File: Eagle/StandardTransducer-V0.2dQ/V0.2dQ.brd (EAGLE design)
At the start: 59.2 x 58 mm, 72 parts, among them CON1 SPI, IC2 TL072D, IC3 LP298XS, IC4 LORA-RA_01_SOIC, J1 87758-0216, Q1 FDN360P, Q2 FDN360P, Q3 FDN360P, Q5 BSP75, U1 RN2483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

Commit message: New version of 0.2dQ
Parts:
- removed C6: 0.1uF, rcl:C0805
- removed L2: 10uH, rcl:L1812
- added Q4: FDN360P, transistor-power:SUPER-SOT3
- added R14: 1k, rcl:R0805
- added R19: 220k, rcl:R0805
- moved RK6 132.6 mm to (40.4, 42.9), turned to 90 degrees
- moved Q5 125.9 mm to (45.7, 43.2)
- moved SJ5 102.0 mm to (18.3, 33.7), turned to 180 degrees
- moved SJ4 102.0 mm to (39.9, 29.5), turned to 90 degrees
- moved Q3 73.1 mm to (7.24, 19.3), flipped to the bottom, turned to 270 degrees
- moved R18 67.3 mm to (10.4, 19.1), flipped to the bottom, turned to 270 degrees
- moved R16 63.6 mm to (8.51, 22.1), flipped to the bottom
- moved C10 10.4 mm to (48.8, 15.4), flipped to the bottom
- moved D2 8.92 mm to (50.5, 16.2)
- moved JP5 8.50 mm to (44.5, 21.3)
- moved F1 6.02 mm to (46.0, 15.5), turned to 270 degrees
- moved D4 5.67 mm to (46.0, 15.5)
- moved R4 1.57 mm to (13.6, 22.9), flipped to the bottom
- moved R5 1.20 mm to (13.2, 19.8), flipped to the bottom, turned to 90 degrees
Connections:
- removed net A3: U$4.39
- removed net DVCC: C6.1, L2.2, Q3.2, R10.1, R11.2, R12.2, R18.2, R8.1
- removed net N$1: F1.2, L1.1, L2.1
- new net AVCCOPA: IC2.8, Q4.3
- new net N$3: Q4.1, R14.1, R19.1
- new net VIN: C11.1, F1.2, IC3.1, J1.2, L1.1, R10.1, R11.2, R12.2, R8.1
- net ANGND: now also IC4.P$16, IC4.P$2, JP5.4
- net AVCC: now also Q4.2, R19.2; no longer IC2.8
- net D+3V3: now also Q3.2, R18.2, U$4.39
- net D10*: now also U$4.31; no longer U$4.30
- net D6*: now also U$4.28; no longer U$4.27
- net D7*: now also U$4.27; no longer U$4.1
- net D8*: now also U$4.29; no longer U$4.28
- net D9*: now also U$4.30; no longer U$4.29
- net GND: no longer C6.2, IC4.P$16, IC4.P$2, JP5.4
- net RA1/2483: now also U$4.1; no longer U$4.31
- net VCC: no longer C11.1, IC3.1, J1.2
- net VOPA: now also R14.2
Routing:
- net VIN: track 0.00 -> 145.8 mm, vias 0 -> 3
- net DVCC: track 143.3 -> 0.00 mm, vias 5 -> 0
- net VCC: track 136.2 -> 22.6 mm, vias 4 -> 1
- net AVCCOPA: track 0.00 -> 72.0 mm
- net TX: track 76.8 -> 34.6 mm, vias 6 -> 2
- net RX: track 69.3 -> 32.6 mm, vias 4 -> 1
- net SVANALOG: track 0.00 -> 22.1 mm, vias 0 -> 1
- net DVSENSORS: track 0.00 -> 20.7 mm, vias 0 -> 1
- net D7*: track 0.00 -> 20.3 mm
- net VSENSORS: track 66.4 -> 48.1 mm, vias 1 -> 0
- net ANGND: track 2.85 -> 18.4 mm, vias 0 -> 5
- net VOPA: track 0.00 -> 14.0 mm
- net N$1: track 13.2 -> 0.00 mm
- net RST: track 125.4 -> 138.4 mm
- net AVCC: track 45.6 -> 34.5 mm
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- added copper zone on layer 1, net ANGND
- added copper zone on layer 16, net ANGND
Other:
- board text added: "GND/AGND"
- board text added: "LORA/BLE"
- board text added: "RA1/2483"
- board text added: "RST"
- board text added: "StandTransducer V2.0"
- board text removed: "StandTransducer V1.0"

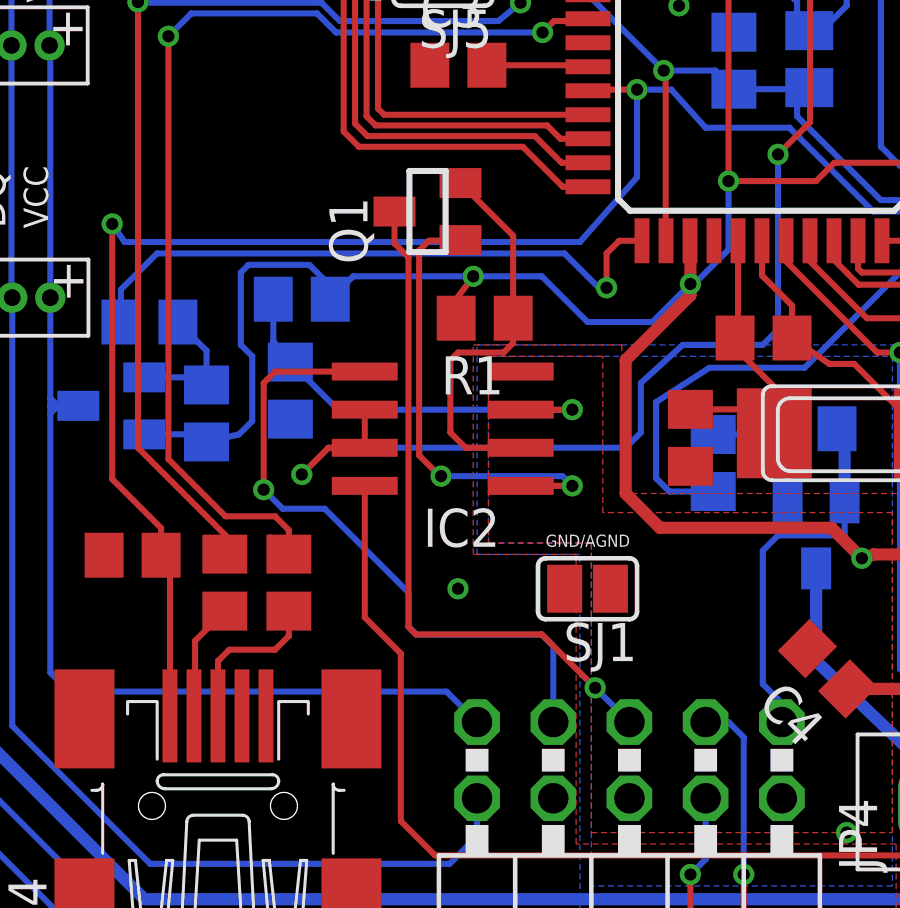
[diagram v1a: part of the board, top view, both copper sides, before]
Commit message: Change width to 16 mil for SVANALOG route.
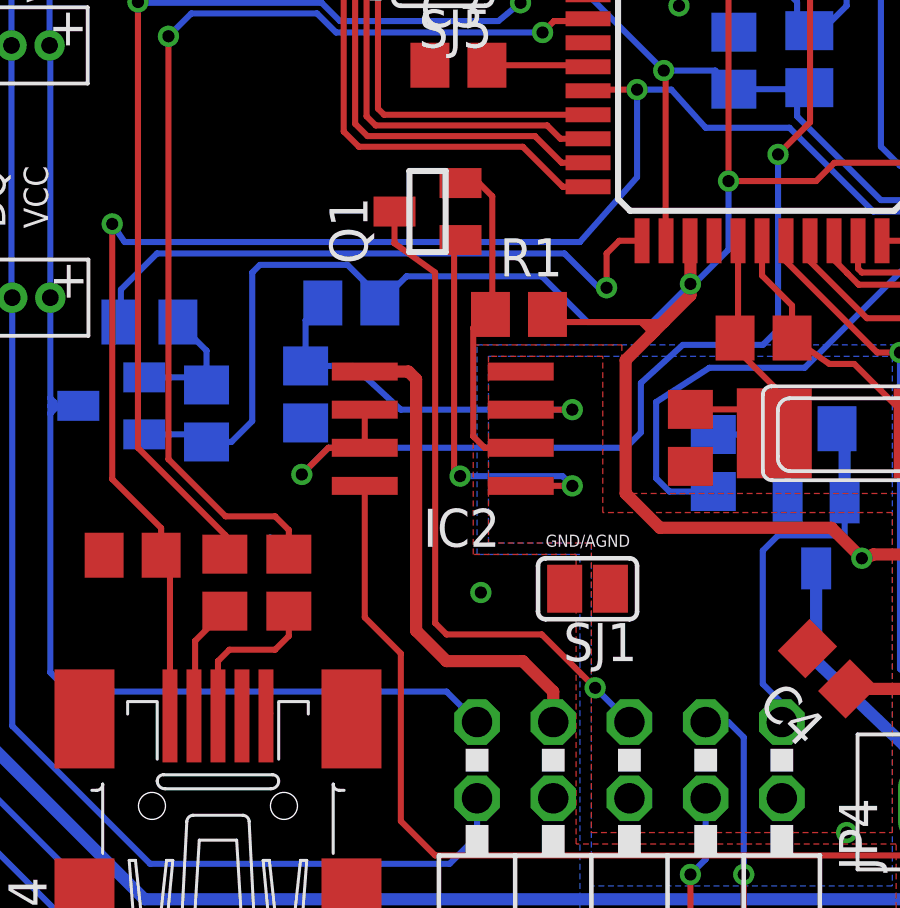
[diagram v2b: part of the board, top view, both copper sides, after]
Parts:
- moved R4 1.66 mm to (15.2, 22.7)
- moved R1 1.15 mm to (20.8, 22.4), turned to 0 degrees
- moved R5 0.52 mm to (13.7, 19.7)
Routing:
- net SVANALOG: track 22.1 -> 16.6 mm, vias 1 -> 0
- net D+3V3: track 189.5 -> 192.3 mm, vias 11 -> 10
- net N$5: track 13.4 -> 11.3 mm
- net N$2: track 15.6 -> 13.6 mm
- net N$4: track 14.1 -> 13.5 mm

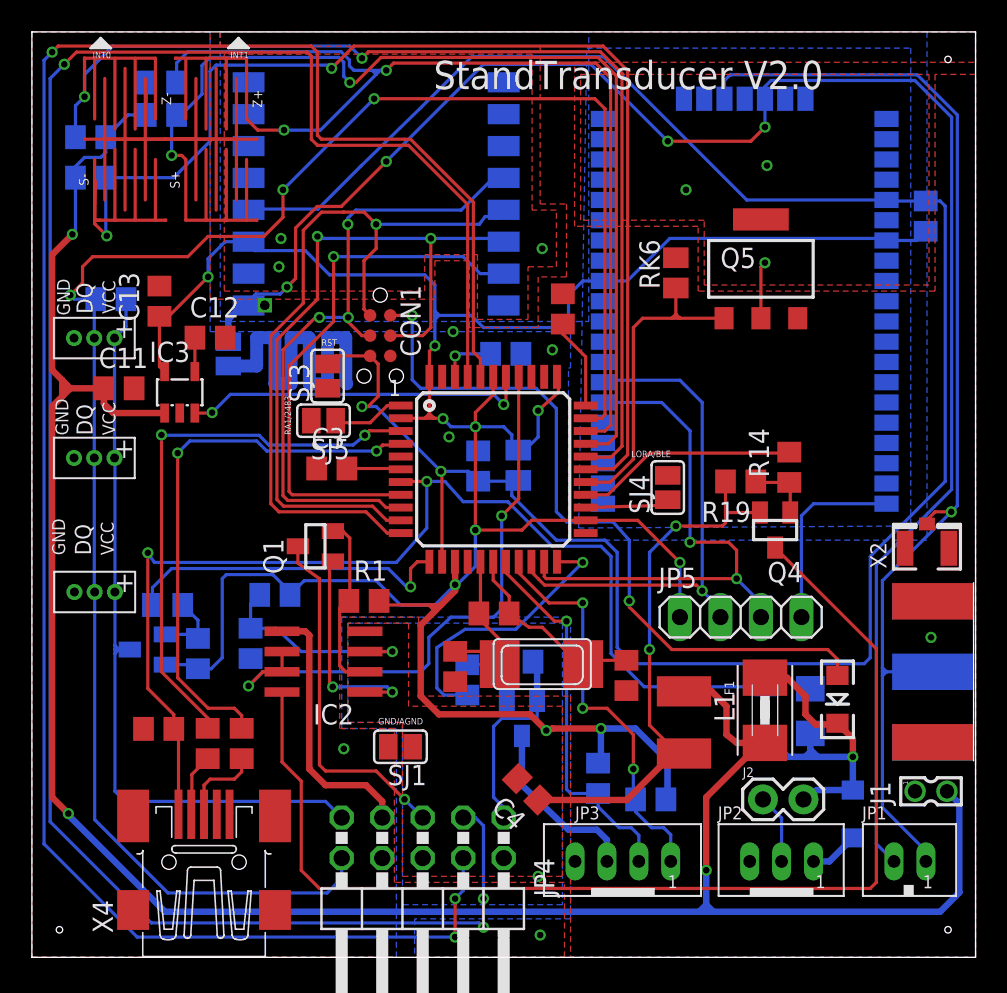
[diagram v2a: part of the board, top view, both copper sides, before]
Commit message: Changes width for VCCOPA and SVANALOG
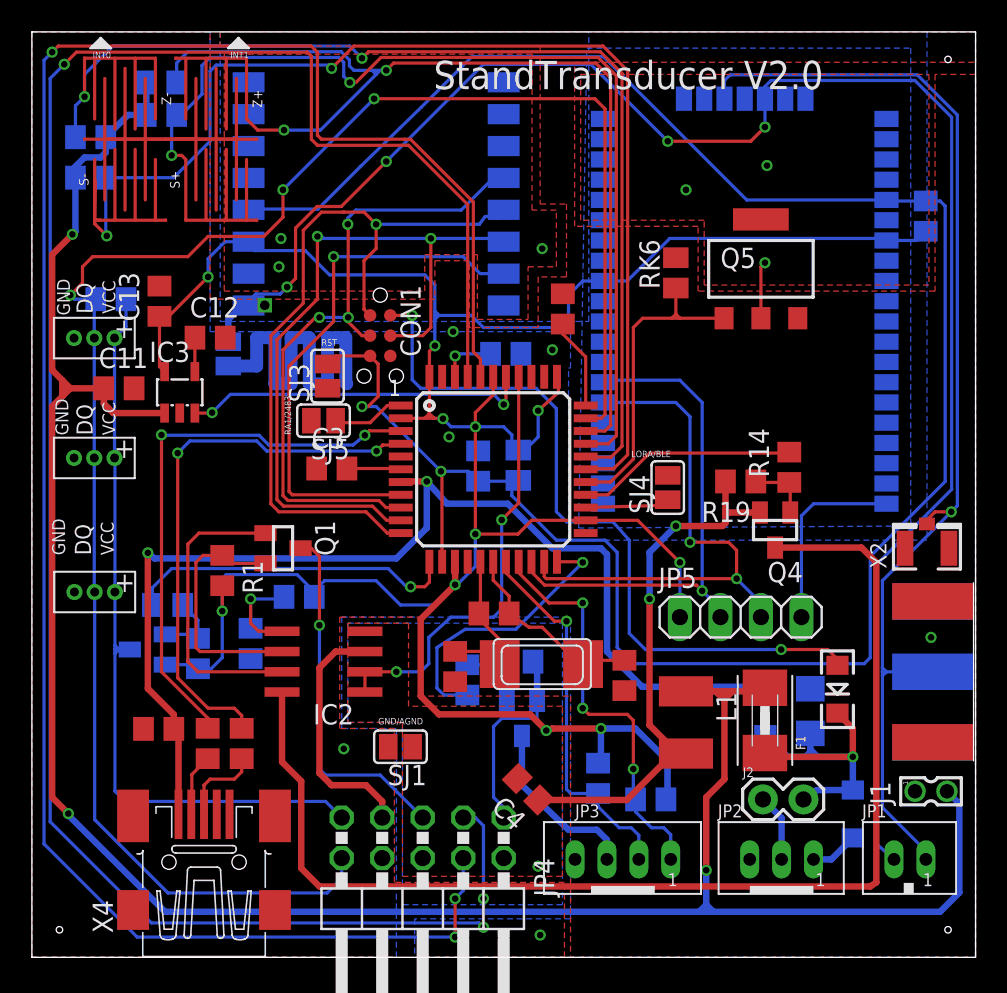
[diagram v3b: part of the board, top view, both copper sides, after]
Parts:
- moved R1 9.09 mm to (11.9, 24.3), turned to 270 degrees
- moved Q1 2.04 mm to (15.7, 25.7), turned to 270 degrees
- moved R4 1.53 mm to (16.8, 22.6)
- moved D2 0.64 mm to (50.5, 16.8)
- moved F1 0.63 mm to (46.0, 14.9), turned to 90 degrees
- moved L1 0.13 mm to (41.0, 14.7)
- moved JP1 0.13 mm to (55.0, 6.10)
- moved JP2 0.13 mm to (47.0, 6.10)
- moved JP3 0.13 mm to (37.1, 6.10)
- moved C8 0.13 mm to (37.2, 17.7)
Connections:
- removed net N$2: IC2.1, Q1.1
- new net N$1: IC2.7, Q1.1
- net N$4: now also IC2.5; no longer IC2.3
- net N$5: now also IC2.6; no longer IC2.2
- net SVANALOG: now also IC2.3; no longer IC2.5
- net VANALOG: now also IC2.1, IC2.2; no longer IC2.6, IC2.7
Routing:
- net N$1: track 0.00 -> 18.7 mm
- net N$2: track 13.6 -> 0.00 mm, vias 2 -> 0
- net VANALOG: track 37.5 -> 27.4 mm
- net N$4: track 13.5 -> 7.67 mm
- net N$5: track 11.3 -> 15.6 mm
- net D+3V3: track 192.3 -> 189.1 mm, vias 10 -> 11
- net AVCCOPA: track 72.0 -> 75.0 mm
- net VIN: track 145.8 -> 146.9 mm
- net SVANALOG: track 16.6 -> 15.6 mm
- net TX: track 34.6 -> 35.1 mm

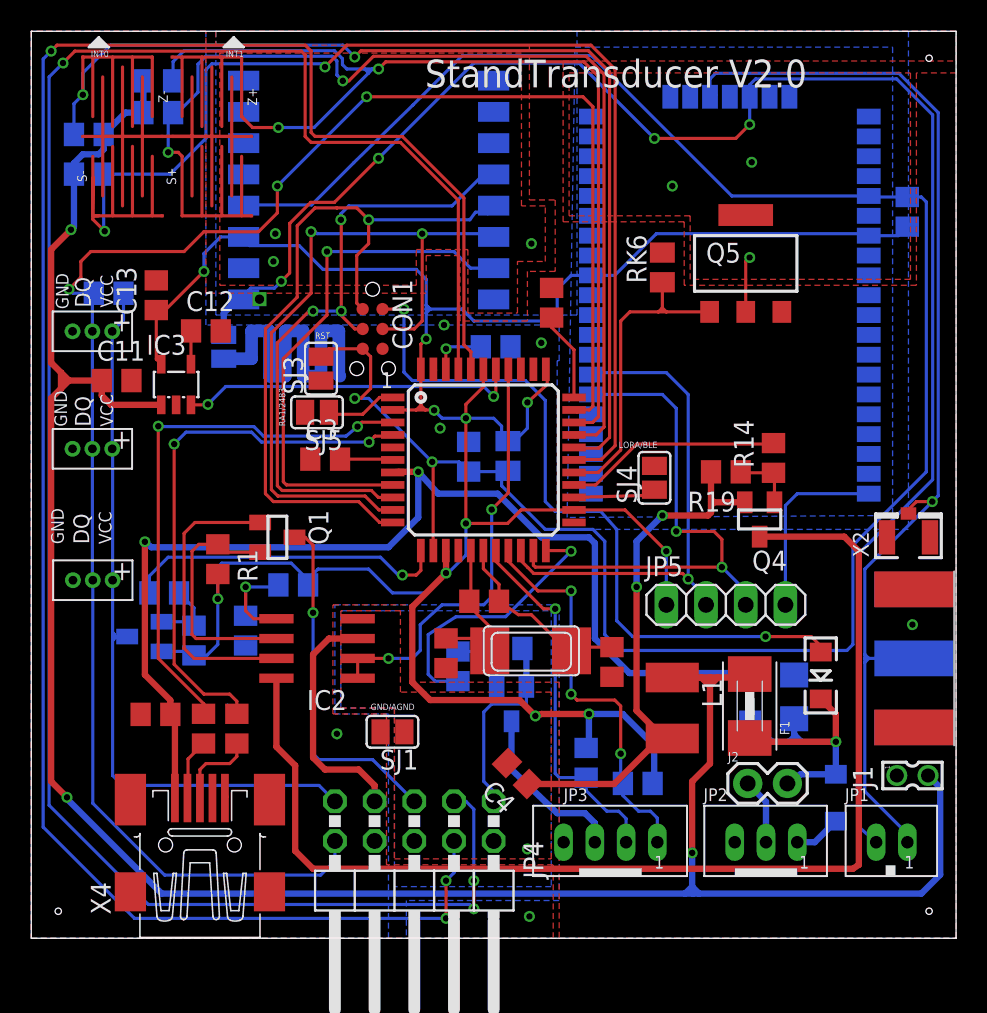
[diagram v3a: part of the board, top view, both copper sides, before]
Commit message: EN pin of LP298SX is connect to VIN pin.
- Delete sheets 2, 3 and 4 and paste all the components and connections to sheet 1.
- EN pin is connect to VIN pin for LP298SX to ensure that microcontroller have power source.
- Change width for all route of D+3V3.
- Change conections for TL072D to minimize route and vias for SVANALOG.
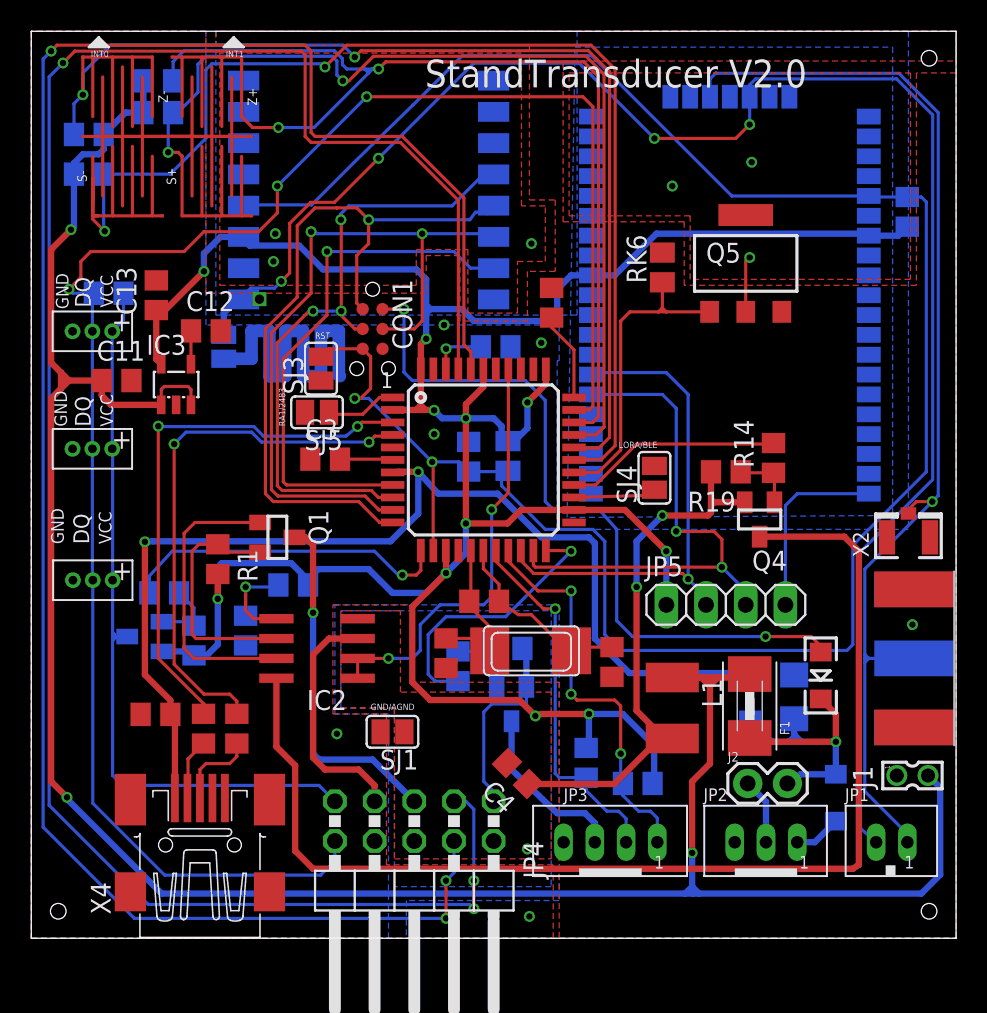
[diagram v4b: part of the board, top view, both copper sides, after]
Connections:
- net ENREG: no longer IC3.3
- net VIN: now also IC3.3
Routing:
- net ENREG: track 21.9 -> 0.00 mm, vias 2 -> 0
- net VIN: track 146.9 -> 151.0 mm

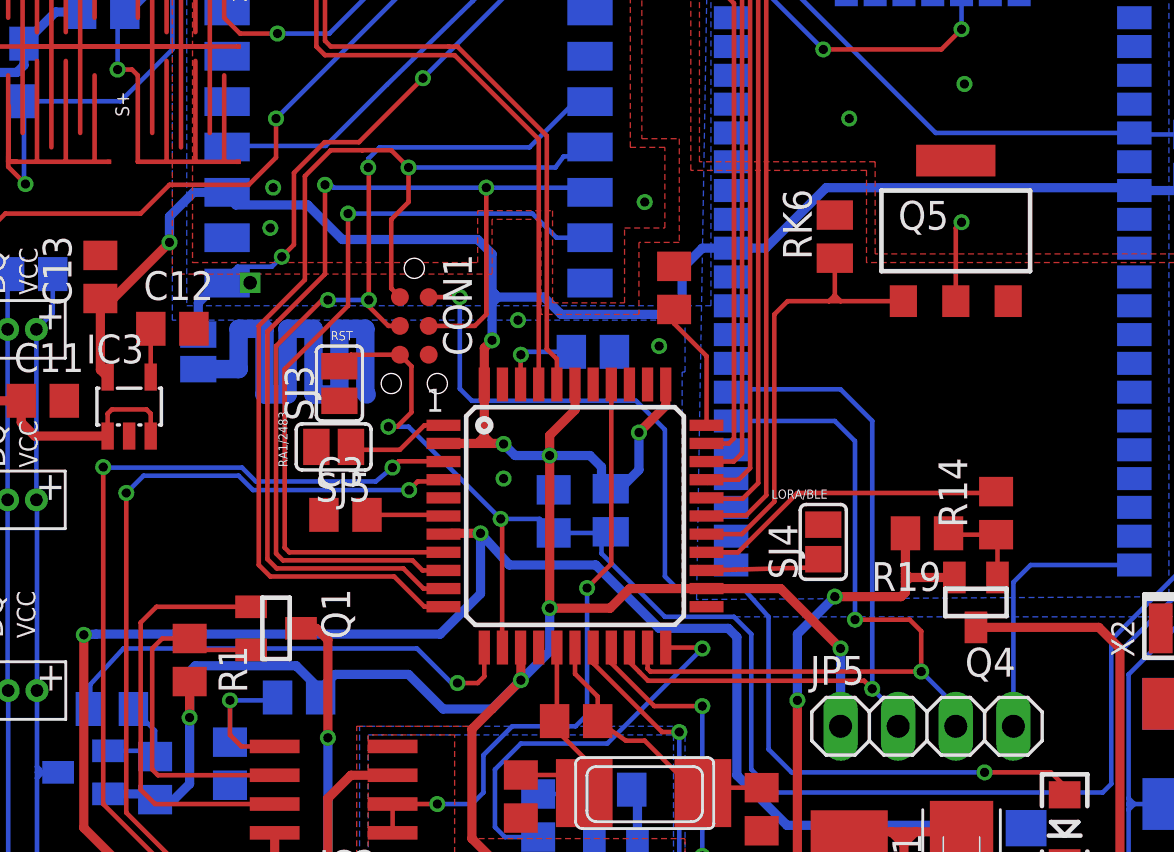
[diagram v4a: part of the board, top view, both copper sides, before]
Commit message: Update ICs and routes.
Changes made:
- BSP75 (BSP613P) to BSP75N.
- FDN 360P to FDN340P (logic level).
- LP298SX to LP5907 (250 mA).
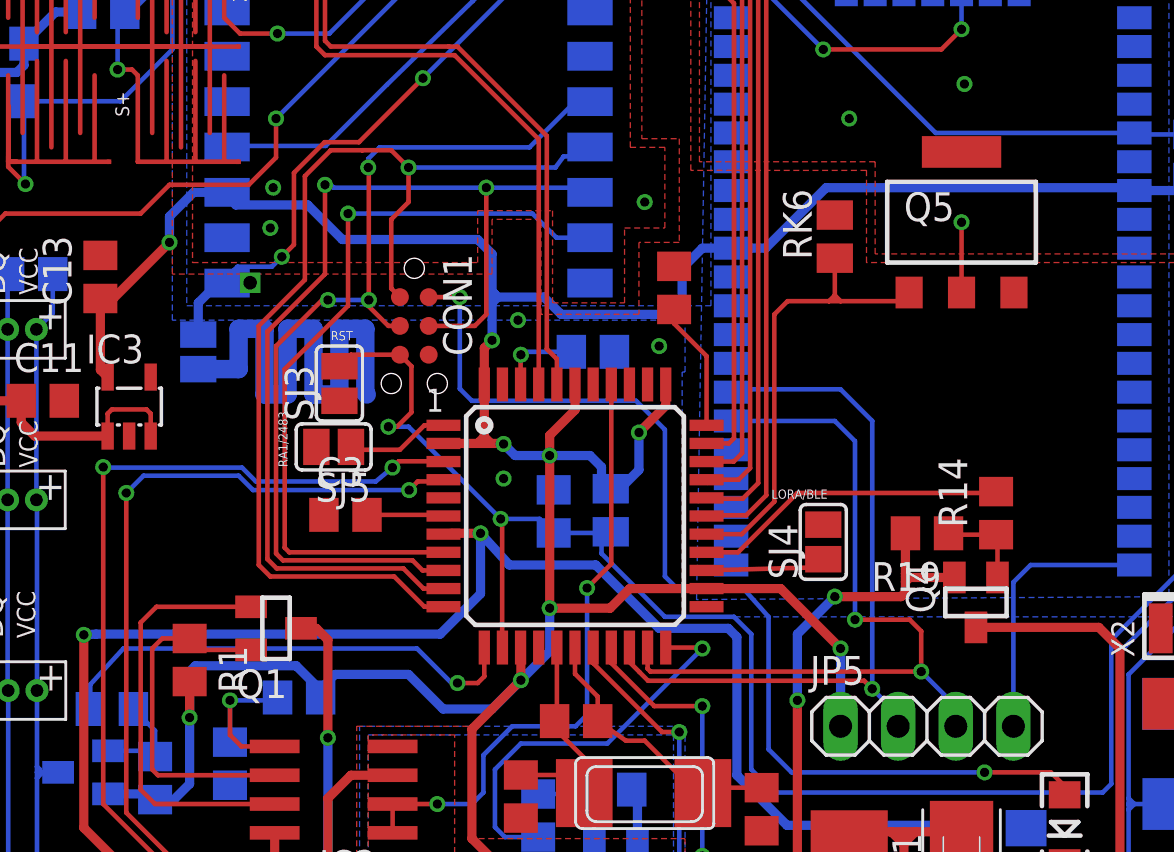
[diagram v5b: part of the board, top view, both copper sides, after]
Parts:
- removed C12: 10nF, rcl:C0805
- IC3: value LP298XS -> LP5907; device adafruit:SOT23-5L -> LP5907:SOT23-5L
- Q1, Q2, Q3, Q4: value FDN360P -> FDN340P; device transistor-power:SUPER-SOT3 -> FDN340P:SUPER-SOT3
- Q5: value BSP75 -> BSP75N; device infineon:PG-SOT-223 -> BSP75N:PG-SOT223-4
- moved Q5 0.46 mm to (46.0, 43.6)
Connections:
- removed net N$6: C12.1, IC3.4
- net GND: no longer C12.2
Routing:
- net N$6: track 2.13 -> 0.00 mm
